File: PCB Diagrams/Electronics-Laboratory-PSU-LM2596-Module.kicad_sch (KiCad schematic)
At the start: 17 parts, among them J1 Bornier 01x02, J10 Conn_01x03, J11 Conn_01x02, J12 Conn_01x01, J2 Bornier 01x02, J3 Conn_01x01, J4 Conn_01x01, J5 Conn_01x01, J6 Conn_01x01, J7 Conn_01x03, J8 Conn_01x03, J9 Conn_01x03

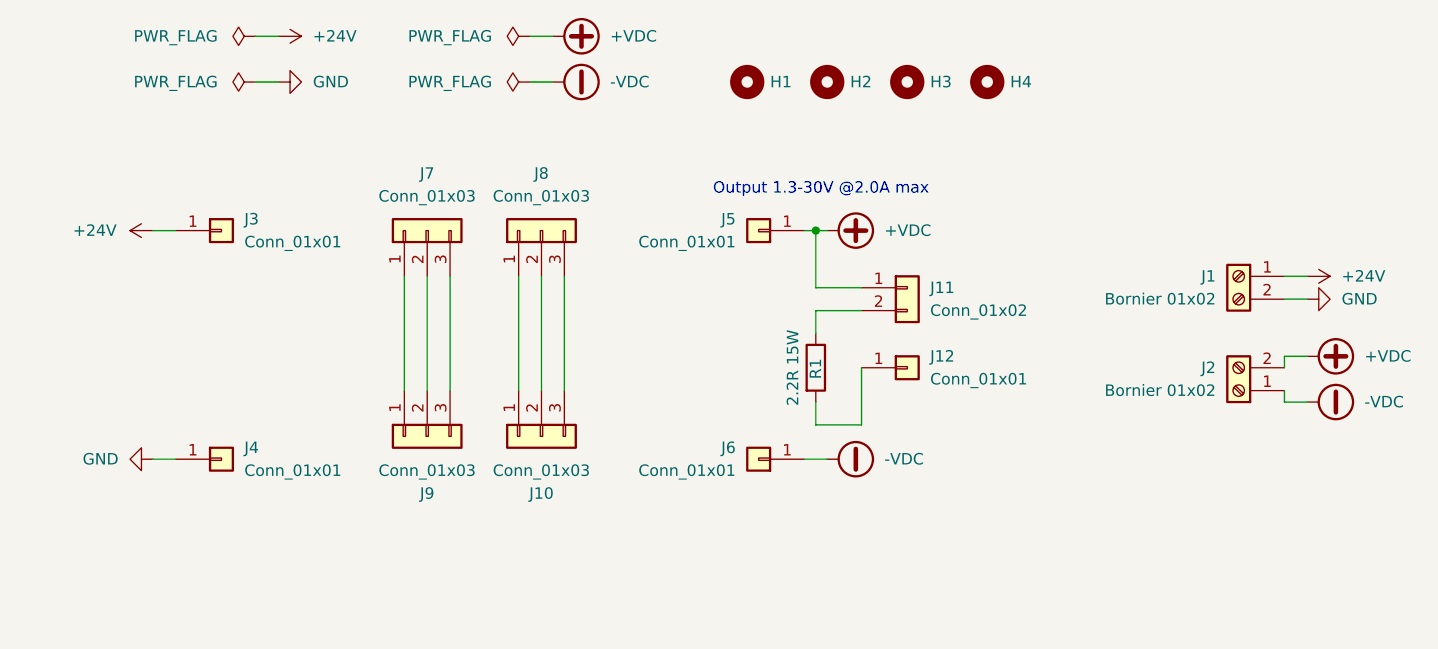
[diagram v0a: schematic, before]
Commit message: update electronic diagrams, adding case 3D model
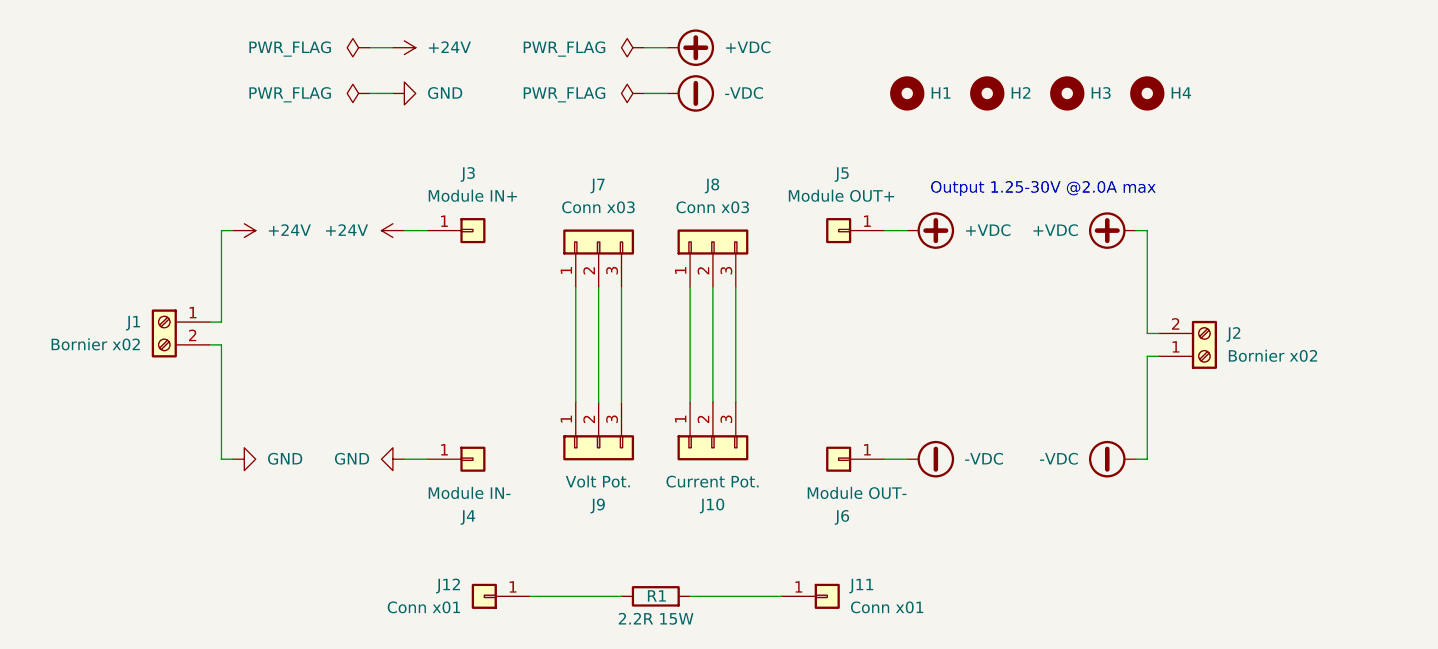
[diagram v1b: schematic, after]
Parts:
- J1, J2: value Bornier 01x02 -> Bornier x02
- J10: value Conn_01x03 -> Current Pot.
- J11: value Conn_01x02 -> Conn x01; footprint Connector_PinHeader_2.54mm:PinHeader_1x02_P2.54mm_Vertical -> Connector_PinHeader_2.54mm:PinHeader_1x01_P2.54mm_Vertical; symbol Connector_Generic:Conn_01x02 -> Connector_Generic:Conn_01x01
- J12: value Conn_01x01 -> Conn x01
- J3: value Conn_01x01 -> Module IN+
- J4: value Conn_01x01 -> Module IN-
- J5: value Conn_01x01 -> Module OUT+
- J6: value Conn_01x01 -> Module OUT-
- J7, J8: value Conn_01x03 -> Conn x03
- J9: value Conn_01x03 -> Volt Pot.
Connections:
- net +VDC: no longer J11.1 (Pin_1)
- net at R1.1: now also J12.1 (Pin_1); no longer J11.2 (Pin_2)
- net at R1.2: now also J11.1 (Pin_1); no longer J12.1 (Pin_1)
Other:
- note added: "Output 1.25-30V @2.0A max"
- note removed: "Output 1.3-30V @2.0A max"
- moved on the sheet: H1, H2, H3, H4, J1, J10, J12, J2, J3, J4, J5, J6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
